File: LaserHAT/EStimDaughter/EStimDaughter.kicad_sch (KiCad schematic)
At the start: 58 parts, among them J1 ELECTRODE E1/E2, J8 J8 power/timing (underside), J9 J9 I2C/release (underside), U1 ISO7741FDBQR, U2 TLV76050DBZR, U4 DAC60501ZDGSR, U5 OPA2192IDGKR, U6 74HC4053BQ, U7 DG419BDQ, U8 LM393DGKR, U9 ISO1640BDR

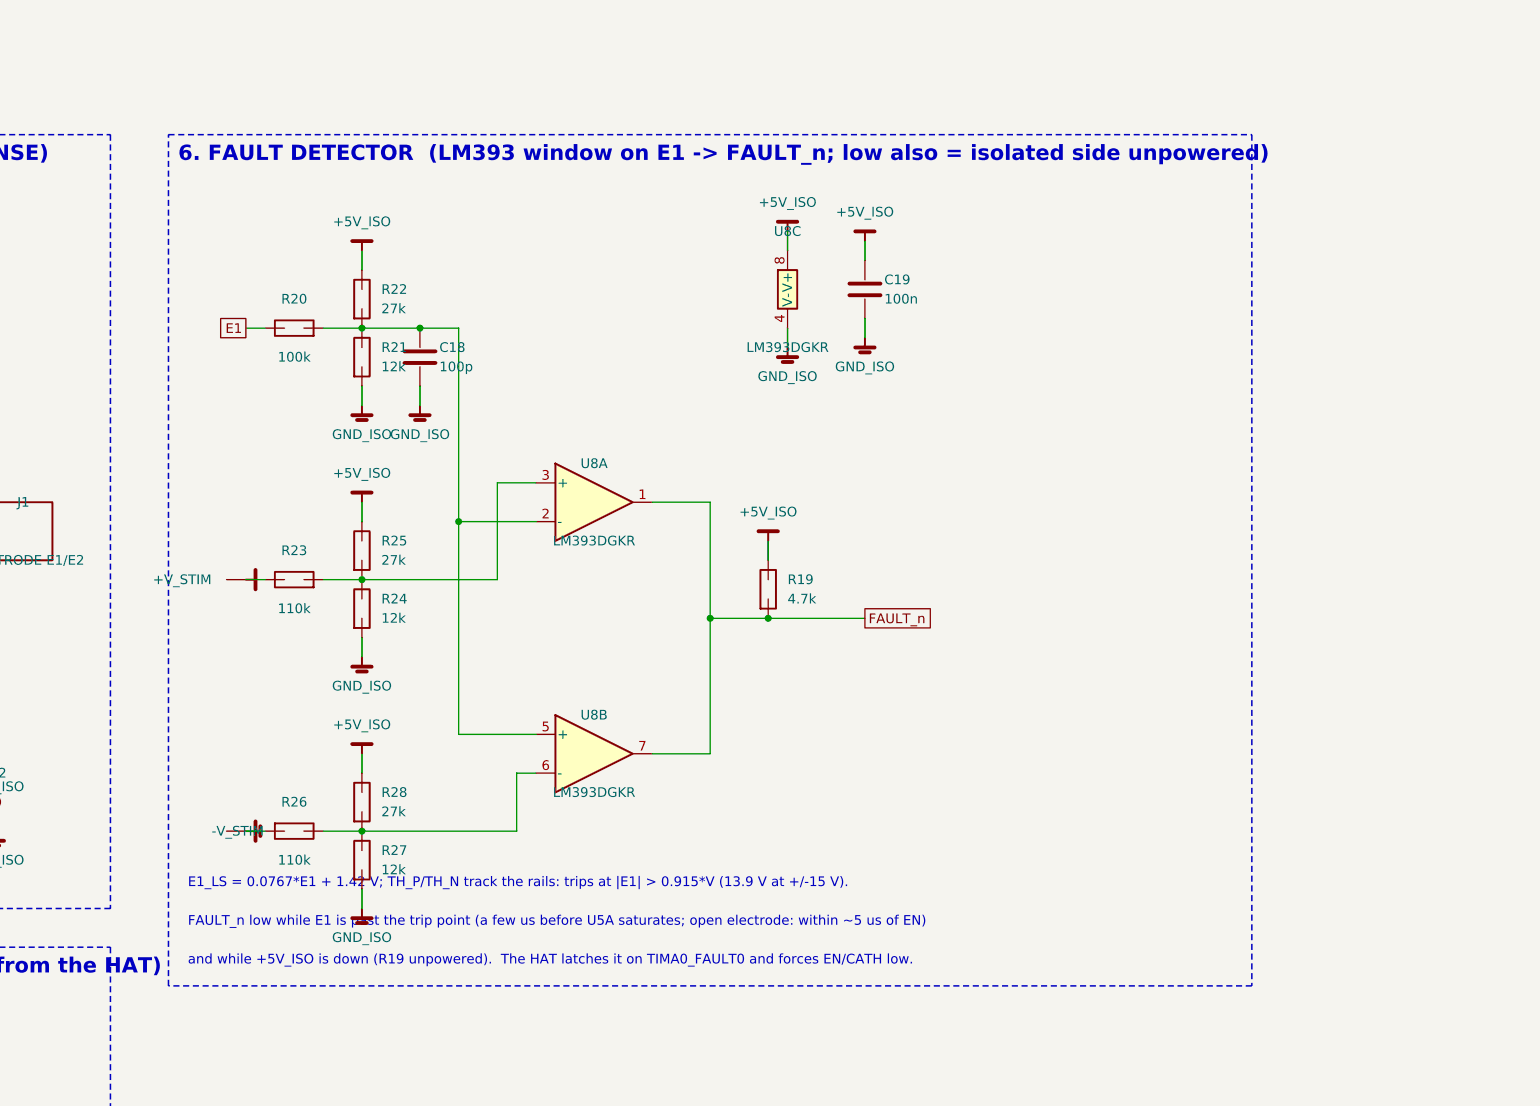
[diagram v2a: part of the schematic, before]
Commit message: EStimDaughter M4b: fault detector simplified to a TLV1702 window on the +/-V rails
- U8 LM393 (0/5 V, nine resistors) -> TLV1702AIDGKR on +V/-V (rail-to-rail inputs, same
  VSSOP-8 footprint): E1 compared directly with the taps of one 10k / 215k / 10k string
  (R23-R25); outputs through R26 10k with D2 BAT54WS clamping FAULT_n; C19 -> 100n 50V
  across the rails.  Removed R20-R22, C18, R27, R28.  Thresholds +/-0.915 V for equal packs,
  the average margin for unequal packs, fault held with a pack missing.
- sims: behavioural comparator (COMPOC) + level shift; full run: lead 8-13 us, open electrode
  ~1 us, no false trips.  Schematic regenerated (netcheck OK, ERC 0), BOM 50 lines.
- Board (the layout session's file, tracks kept): removed parts deleted, U8/R23-R26/R19
  re-netted and revalued, C19 swapped to 0603, D2 parked east of the outline.
  tools/pcb_sync.py loads footprints through PCB_IO_KICAD_SEXPR (9.0.8 quirk).
- Docs: README, DESIGN_NOTES (M4b), LAYOUT_HANDOFF (open question 1 answered: J9.4 = SDA,
  J9.5 = SCL accepted), spec section 7, REV2_NOTES firmware pins, sim/models README.

Co-Authored-By: Claude Fable 5.1 <noreply@anthropic.com>
Claude-Session: https://claude.ai/code/session_018vgLizGzYPynnY93ajvoVA
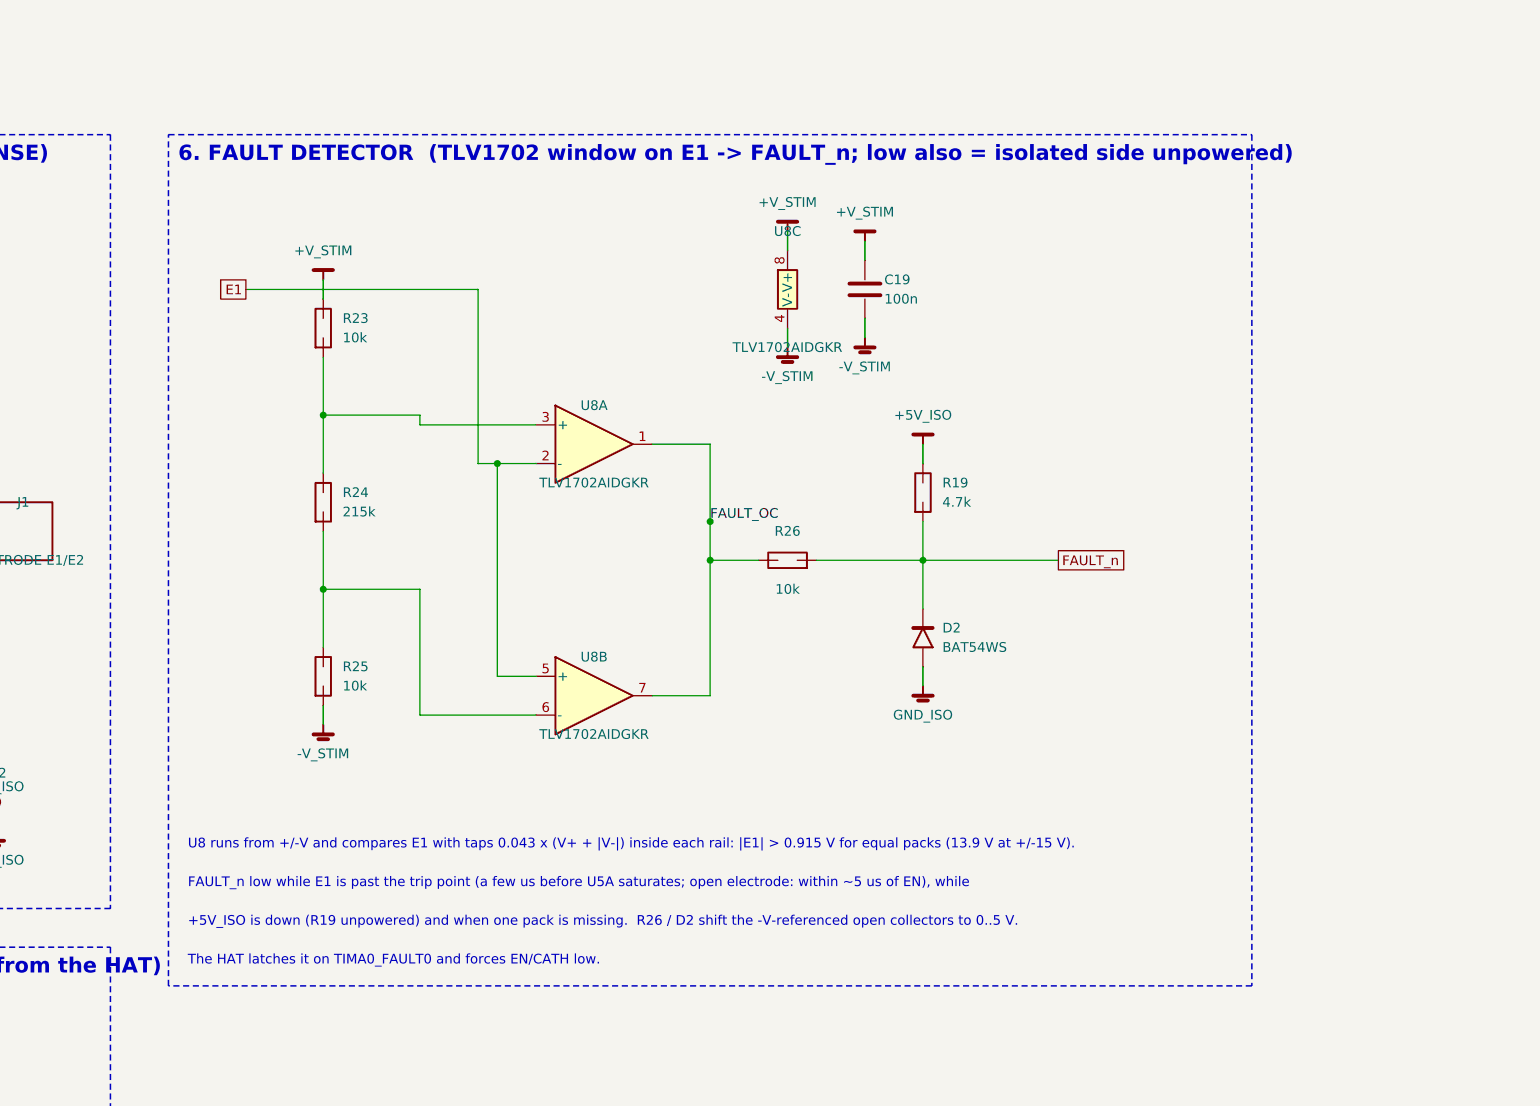
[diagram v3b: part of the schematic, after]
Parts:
- removed C18: 100p, Capacitor_SMD:C_0402_1005Metric, symbol estim:C
- removed R20: 100k, Resistor_SMD:R_0402_1005Metric, symbol estim:R
- removed R21, R27: 12k, Resistor_SMD:R_0402_1005Metric, symbol estim:R
- removed R22, R28: 27k, Resistor_SMD:R_0402_1005Metric, symbol estim:R
- removed U8: LM393DGKR, Package_SO:VSSOP-8_3x3mm_P0.65mm, symbol estim:LM393
- added D2: BAT54WS, Diode_SMD:D_SOD-323, symbol estim:D
- added U8: TLV1702AIDGKR, Package_SO:VSSOP-8_3x3mm_P0.65mm, symbol estim:TLV1702
- C19: footprint Capacitor_SMD:C_0402_1005Metric -> Capacitor_SMD:C_0603_1608Metric; LCSC C1525 -> C14663
- R23, R26: value 110k -> 10k; LCSC C2909311 -> C25744
- R24: value 12k -> 215k; LCSC C25752 -> C185443
- R25: value 27k -> 10k; LCSC C22369538 -> C25744
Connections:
- net +5V_ISO: no longer C19.1, R25.1
- net +V_STIM: now also C19.1, U8.8 (V+)
- net -V_STIM: now also C19.2, R25.2, U8.4 (V-); no longer R26.2
- net E1: now also U8.2 (-), U8.5 (+)
- net FAULT_n: now also R26.2, D2.1 (K)
- net GND_ISO: now also D2.2 (A); no longer C19.2, R24.2
- net at R23.2, R24.1: now also U8.3 (+); no longer R25.2
- net FAULT_OC: now reaches R26.1
- net FAULT_OC: now also U8.1, U8.7
- new net: R24.2, R25.1, U8.6 (-)
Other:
- note added: "+5V_ISO is down (R19 unpowered) and when one pack is missing. R26 / D2 shift the -V-referenced open collectors to 0..5 V."
- note added: "6. FAULT DETECTOR (TLV1702 window on E1 -> FAULT_n; low also = isolated side unpowered)"
- note added: "FAULT_n low while E1 is past the trip point (a few us before U5A saturates; open electrode: within ~5 us of EN), while"
- note added: "The HAT latches it on TIMA0_FAULT0 and forces EN/CATH low."
- note added: "U8 runs from +/-V and compares E1 with taps 0.043 x (V+ + |V-|) inside each rail: |E1| > 0.915 V for equal packs (13.9 V at +/-15 V)."
- note removed: "6. FAULT DETECTOR (LM393 window on E1 -> FAULT_n; low also = isolated side unpowered)"
- note removed: "E1_LS = 0.0767*E1 + 1.42 V; TH_P/TH_N track the rails: trips at |E1| > 0.915*V (13.9 V at +/-15 V)."
- note removed: "FAULT_n low while E1 is past the trip point (a few us before U5A saturates; open electrode: within ~5 us of EN)"
- note removed: "and while +5V_ISO is down (R19 unpowered). The HAT latches it on TIMA0_FAULT0 and forces EN/CATH low."

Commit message: EStimDaughter M4c: ADG1436 switch, U8 units swapped, J8.3/J8.5 = FAULT/EN, 4-layer routed with In2 rail pours
Circuit
- 74HC4053 + the -5 V zener rail (R6, D1, C8) -> one ADG1436YCPZ (LFCSP-16 4x4, +/-15 V dual SPDT):
  switch 1 (IN1 = EN) gates 0 V / SW_P -> V_IN, switch 2 (IN2 = CATH) picks VSET_P / VSET_N -> SW_P;
  EN pin on VDD (+V_STIM). C13/C14 are 100 n 50 V +/-V taps; C4 and C20 dropped, C2 serves both
  isolator VCC2 pins. -V rail load now ~1.5 mA: below the Mornsun A0515S minimum, RECOM RB-0515D/HP
  or batteries are unaffected.
- U8 comparator halves swapped (B = TH_P edge). U1 channels A/B/C = RELEASE/EN/CATH.
- Connector standard: J8.3 = FAULT_n (PA6, TIMA0_FAULT0), J8.5 = EN (PA7); J9.4 = SDA, J9.5 = SCL.
  HAT copper and the laser module must follow: spec section 3/7 and LAYOUT_HANDOFF open questions.

Schematic generator
- Deterministic UUIDs (uuid5 of the reference); footprints carry KiCad's root-sheet paths, full
  Lib:Name FPIDs and the schematic's net names, so F8 is a no-op. VSET_P / VSET_N labelled.

Board
- Outline y 76-109. 4 layers: F parts/signals + GND pours, In1 split GND planes, In2 power
  (user-routed 0.8 mm traces plus generated per-rail pours shaped by that routing), B logic runs.
- Decoupling moved onto pins (C10 at U4, C11/C12 at U5/U7, C2 between U1/U9); labels back on
  board; DRC: 0 unconnected, 0 electrical errors, schematic parity clean.

Co-Authored-By: Claude Fable 5.1 <noreply@anthropic.com>
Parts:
- removed C20: 100n, Capacitor_SMD:C_0402_1005Metric, symbol estim:C
- removed C4, C8: 1u 50V, Capacitor_SMD:C_0603_1608Metric, symbol estim:C
- removed D1: BZT52C4V7S, Diode_SMD:D_SOD-323, symbol estim:D_Zener
- removed R6: 1.5k, Resistor_SMD:R_0603_1608Metric, symbol estim:R
- removed U6: 74HC4053BQ, Package_DFN_QFN:DHVQFN-16-1EP_2.5x3.5mm_P0.5mm_EP1x2mm, symbol estim:74HC4053
- added U6: ADG1436YCPZ, Package_DFN_QFN:QFN-16-1EP_4x4mm_P0.65mm_EP2.5x2.5mm, symbol estim:ADG1436
- C13, C14: footprint Capacitor_SMD:C_0402_1005Metric -> Capacitor_SMD:C_0603_1608Metric; LCSC C1525 -> C14663
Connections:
- net -5V_ISO is gone; now on net -V_STIM: C14.2
- net +5V_ISO: no longer C13.1
- net +V_STIM: now also C13.1, U6.11 (VDD), U6.12 (EN)
- net -V_STIM: now also U6.17 (EP), U6.3 (VSS)
- net CATH: now also U1.12 (OUTC), U6.6 (IN2); no longer U1.13 (OUTB)
- net CATH_H: now also U1.5 (INC); no longer U1.4 (INB)
- net E1: now also U8.3 (+), U8.6 (-); no longer U8.2 (-), U8.5 (+)
- net EN: now also U1.13 (OUTB), U6.15 (IN1); no longer U1.12 (OUTC)
- net EN_H: now also J8.5 (Pin_5), U1.4 (INB); no longer J8.3 (Pin_3), U1.5 (INC)
- net FAULT_H: now also J8.3 (Pin_3); no longer J8.5 (Pin_5)
- net GND_ISO: now also U6.2 (S1B), U6.4 (GND)
- net SW_P: now also U6.16 (S1A), U6.9 (D2)
- net V_IN: now also U6.1 (D1)
- net at R23.2, R24.1: now also U8.5 (+); no longer U8.3 (+)
- net at R24.2, R25.1: now also U8.2 (-); no longer U8.6 (-)
- net VSET_P: now reaches R10.1, U4.2 (VOUT)
- net VSET_P: now also U6.10 (S2B)
- net VSET_N: now reaches R11.2, U5.7
- net VSET_N: now also U6.8 (S2A)
- no-connect marks 3 -> 7
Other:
- note added: "2. ISOLATED POWER (A0515S +/-15 V, +5 V LDO)"
- note added: "3. SET-POINT (DAC60501 I2C, internal 2.5 V ref / 2 -> 0..1.25 V = VSET_P; U5B inverts -> VSET_N; ADG1436 -> V_IN)"
- note added: "C3 at PS1 pins 1-2, C5 at pin 4 (C6, the LDO input cap, is the +V bulk). Load: +V ~9 mA (LDO -> U1, U9, U4), -V ~1.5 mA (U5, U8): below the 10 % minimum load"
- note added: "Decoupling at: C10 U4 VDD, C9 U4 VREFIO, C13/C14 (+/-V) on the west feed near U6. DAC60501Z: I2C address 0x48; write GAIN (0x04) = 0x0100 first, then DAC (0x08) = code << 4."
- note added: "Firmware: set CATH before raising EN, hold it until EN falls. ADG1436 EN pin tied high: EN low would float V_IN."
- note added: "J8 (underside): 1 GND, 2 +5V, 3 FAULT_n (HAT PA6), 4 PWM_B=CATH, 5 PWM_A=EN. J9: 1 GND, 2 +3V3, 3 RELEASE, 4 SDA, 5 SCL."
- note added: "R7/R8: I2C pull-ups, HAT side. C1 at U1 pin 1, C2 between U1 pin 16 and U9 pin 5 (both VCC2), C17 at U9 pin 4."
- note added: "VSET_P = 0..1.25 V. U6 sw 2: CATH picks VSET_P (0) / VSET_N (1) -> SW_P; sw 1: EN picks 0 V (0) / SW_P (1) -> V_IN. EN low (isolator fail-safe) = zero current."
- note added: "of the Mornsun A0515S on the -V rail since the -5 V zener chain went (M4c); fit the RECOM RB-0515D/HP (0 % min load) or batteries."
- note removed: "2. ISOLATED POWER (A0515S +/-15 V, +5 V LDO, -4.7 V zener)"
- note removed: "3. SET-POINT (DAC60501 I2C, internal 2.5 V ref / 2 -> 0..1.25 V = VSET_P; U5B inverts -> VSET_N; 74HC4053 -> V_IN)"
- note removed: "C3 at PS1 pins 1-2, C4/C5 at pins 4-6. PS1 needs >= 10 % load per rail (~3.4 mA): U1, U2, U4, U5, U6, U8, U9, D1 draw ~9 mA."
- note removed: "Decoupling at: C10 U4 VDD, C9 U4 VREFIO, C13/C14 U6. DAC60501Z: I2C address 0x48; write GAIN (0x04) = 0x0100 first, then DAC (0x08) = code << 4."
- note removed: "Firmware: set CATH before raising EN, hold it until EN falls. Switch 3 unused (tied to GND)."
- note removed: "J8 (underside): 1 GND, 2 +5V, 3 PWM_A=EN, 4 PWM_B=CATH, 5 GPIO=FAULT_n. J9: 1 GND, 2 +3V3, 3 RELEASE, 4 SDA, 5 SCL."
- note removed: "R7/R8: I2C pull-ups, HAT side. C1 at U1 pin 1, C2 at pin 16, C17/C20 at U9 pins 4/5."
- note removed: "VSET_P = 0..1.25 V. 4053: S1 = CATH picks -VSET / +VSET, S2 = EN picks that or 0 V -> V_IN. EN low (isolator fail-safe) = zero current."
